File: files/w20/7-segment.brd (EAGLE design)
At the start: 37.5 x 64.8 mm, 18 parts

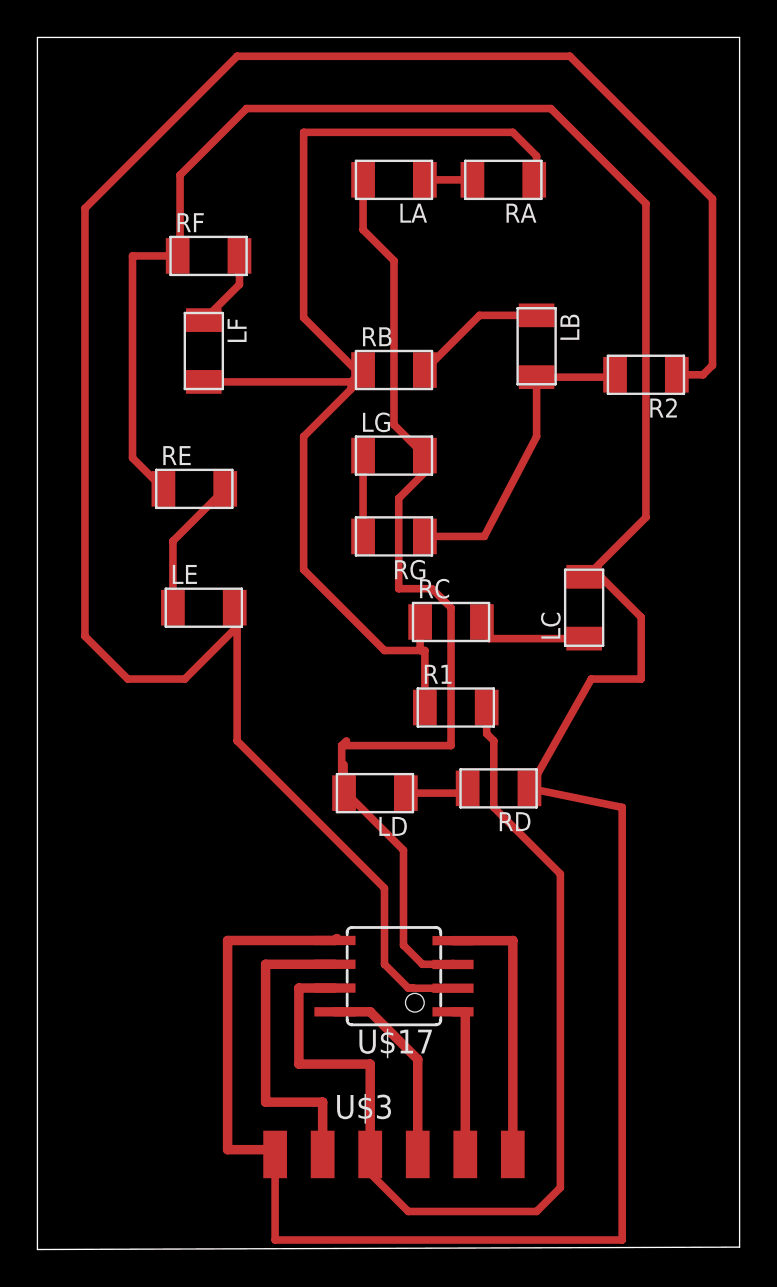
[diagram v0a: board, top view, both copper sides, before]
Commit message: board layout tweaks
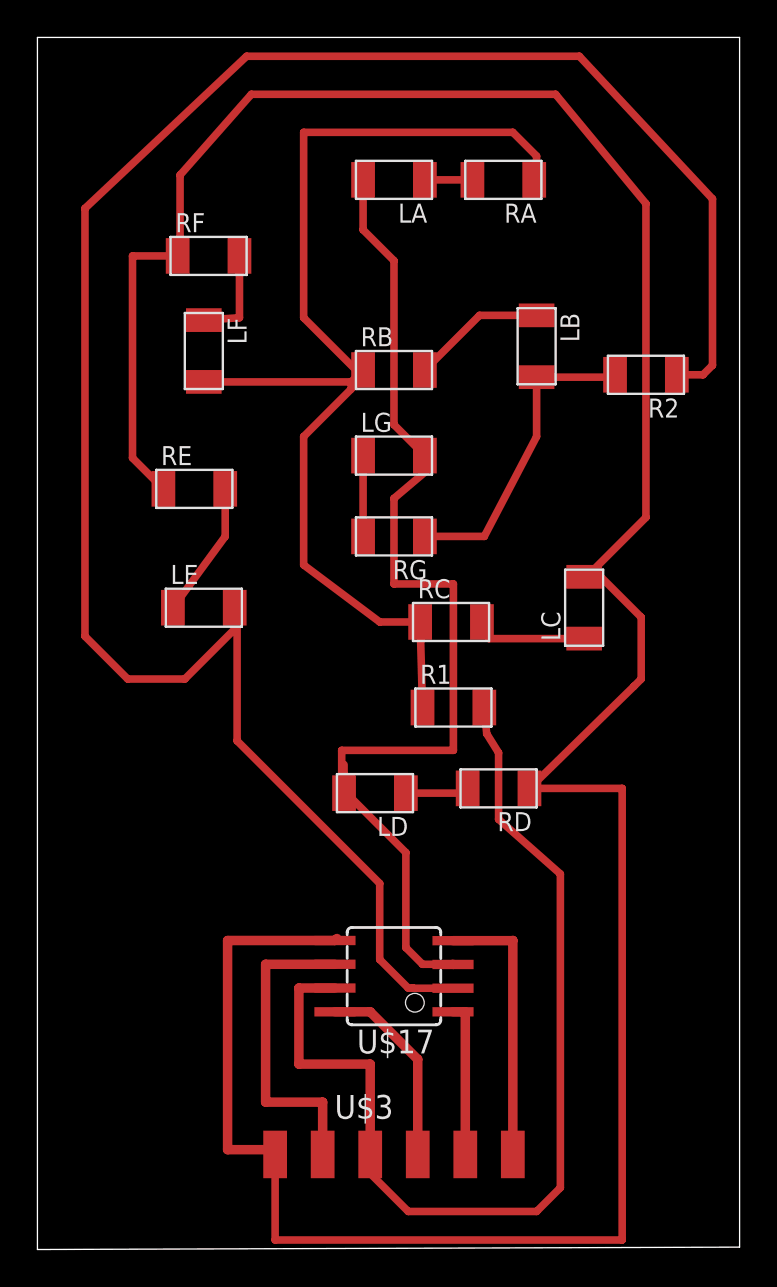
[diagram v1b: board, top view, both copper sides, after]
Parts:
- moved R1 0.13 mm to (20.4, 28.2)
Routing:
- net SCK: track 114.3 -> 113.1 mm
- net MOSI: track 157.4 -> 158.4 mm
- net N$6: track 4.22 -> 5.21 mm
- net PB4: track 56.3 -> 57.2 mm

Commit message: vias done
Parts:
- moved R2 10.8 mm to (27.6, 35.7)
- moved RE 9.11 mm to (7.10, 30.8)
- moved LE 8.94 mm to (11.1, 25.5), turned to 270 degrees
- moved LA 8.43 mm to (18.0, 48.0)
- moved RA 8.41 mm to (23.6, 48.0)
- moved LC 7.78 mm to (26.3, 25.8)
- moved LF 6.99 mm to (9.11, 40.5)
- moved LB 6.10 mm to (25.1, 41.4)
- moved RF 5.91 mm to (9.27, 46.7), turned to 270 degrees
- moved LG 5.05 mm to (18.0, 36.7)
- moved RG 4.75 mm to (18.0, 32.6)
- moved RC 4.44 mm to (18.0, 29.0)
- moved RD 4.20 mm to (23.1, 19.7)
- moved LD 4.00 mm to (16.3, 19.6)
- moved R1 4.00 mm to (18.0, 25.0)
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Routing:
- net MOSI: track 158.4 -> 147.1 mm
- net SCK: track 113.1 -> 102.1 mm
- net PB4: track 57.2 -> 48.7 mm
- net N$3: track 6.05 -> 9.23 mm
- net GND: track 14.6 -> 11.9 mm
- net RST: track 8.28 -> 5.58 mm
- net N$6: track 5.21 -> 3.06 mm
- net VCC: track 10.6 -> 8.70 mm
- net N$2: track 7.18 -> 5.47 mm
- net N$5: track 7.26 -> 5.91 mm
- net MISO: track 16.9 -> 15.8 mm
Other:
- board size 37.5 x 64.8 mm -> 28.5 x 55.8 mm

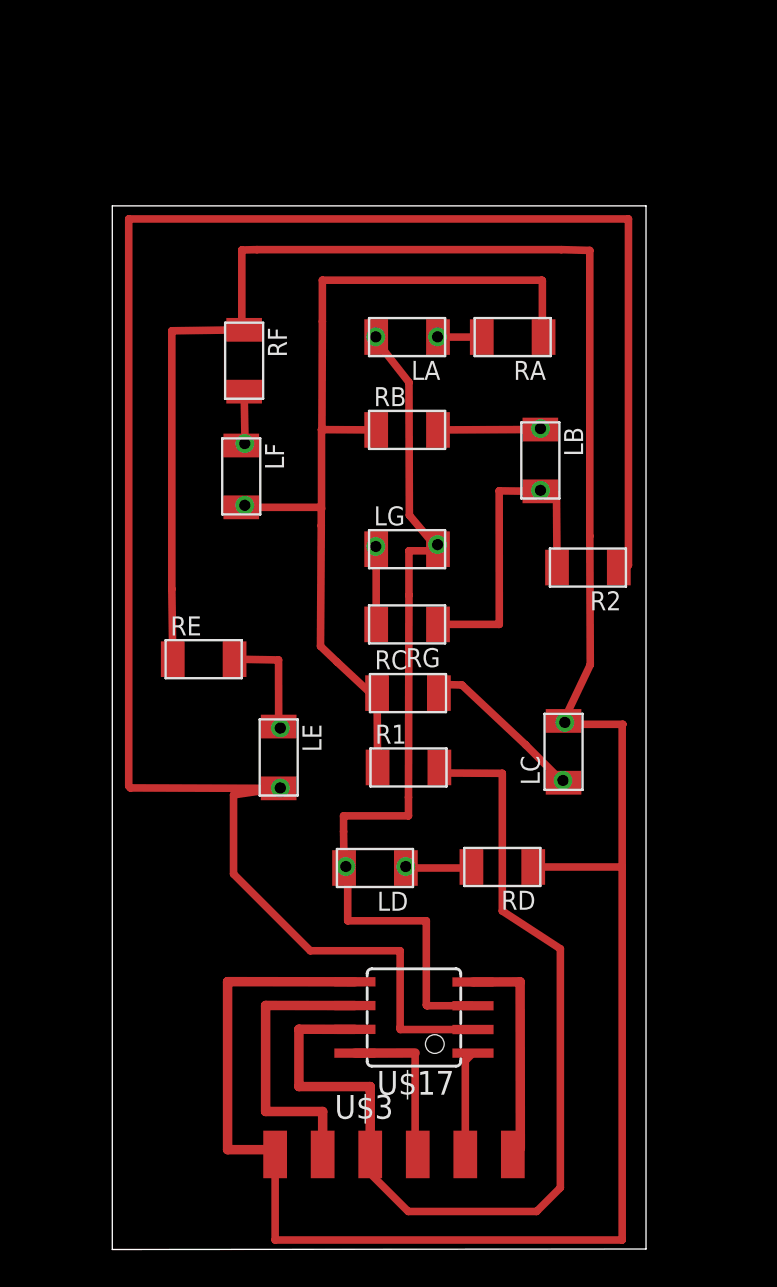
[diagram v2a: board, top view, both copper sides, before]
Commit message: 7segment board refactoring
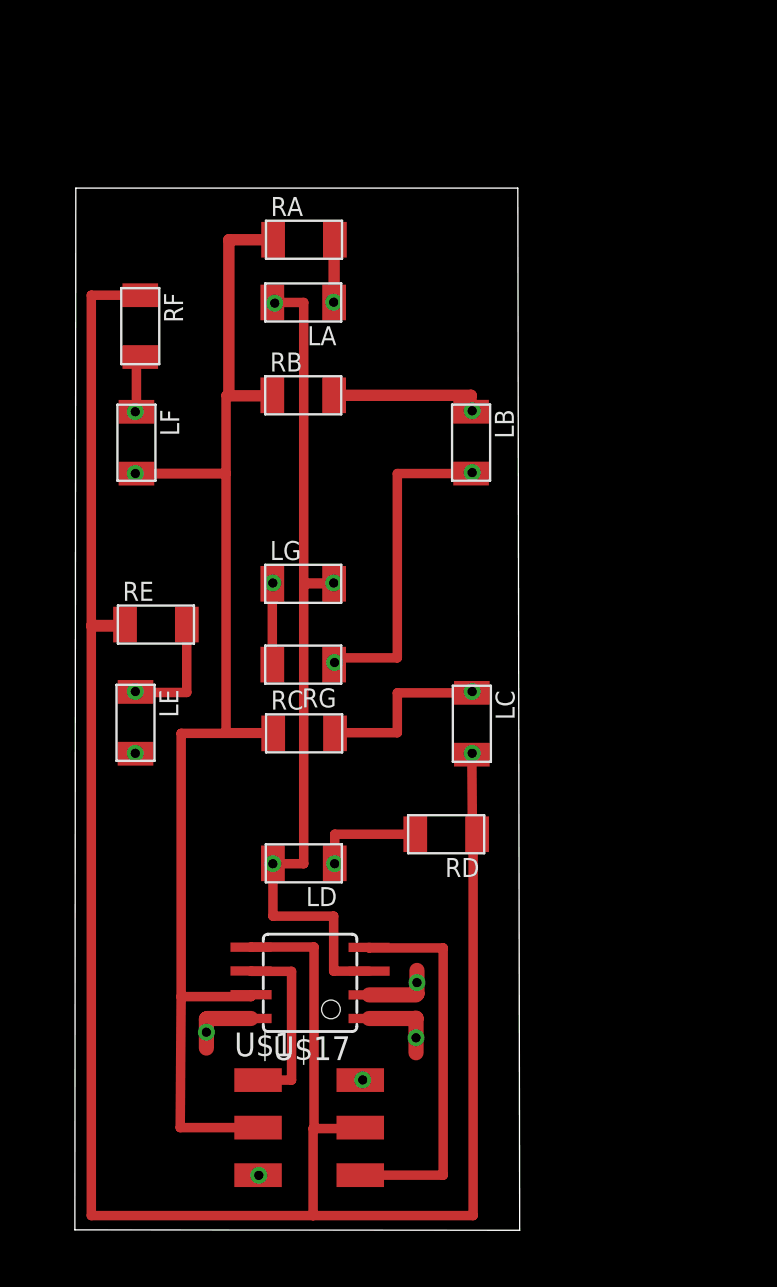
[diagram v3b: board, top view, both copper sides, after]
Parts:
- removed R1, R2: (no value), fab:R1206FAB
- removed U$3: FTDI-SMD-HEADER, fab:1X06SMD
- added U$1: AVRISPSMD, fab:2X03SMD
- moved RA 12.3 mm to (12.5, 53.2), turned to 0 degrees
- moved LE 7.87 mm to (3.46, 27.4)
- moved RG 5.95 mm to (12.4, 30.5)
- moved RC 5.95 mm to (12.5, 26.8)
- moved LF 5.88 mm to (3.51, 42.3)
- moved LA 5.85 mm to (12.4, 49.8)
- moved LG 5.85 mm to (12.4, 34.8)
- moved RB 5.85 mm to (12.4, 44.9)
- moved RF 5.85 mm to (3.72, 48.6)
- moved U$17 5.85 mm to (12.8, 13.5)
- moved LC 5.12 mm to (21.4, 27.3), turned to 270 degrees
- moved LB 3.82 mm to (21.4, 42.3)
- moved LD 3.81 mm to (12.5, 19.9)
- moved RD 3.47 mm to (20.1, 21.4)
- moved RE 3.15 mm to (4.55, 32.6)
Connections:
- net GND: now also U$1.6; no longer U$3.1
- net MISO: now also U$1.1; no longer U$3.5
- net MOSI: now also U$1.4; no longer U$3.6
- net PB3: no longer R2.1, R2.2
- net RST: now also U$1.5; no longer U$3.2
- net SCK: now also U$1.3; no longer R1.1, R1.2, U$3.4
- net VCC: now also U$1.2; no longer U$3.3
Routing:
- net PB3: track 126.8 -> 21.4 mm
- net MOSI: track 147.1 -> 121.5 mm
- net SCK: track 102.1 -> 79.7 mm
- net GND: track 11.9 -> 20.6 mm
- net MISO: track 15.8 -> 9.79 mm
- net VCC: track 8.70 -> 3.97 mm
- net N$2: track 5.47 -> 8.20 mm
- net N$4: track 3.63 -> 5.86 mm
- net RST: track 5.58 -> 4.38 mm
- net PB4: track 48.7 -> 47.5 mm, vias 0 -> 1
- net N$1: track 2.34 -> 3.39 mm
- net N$3: track 9.23 -> 9.99 mm
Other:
- board size 28.5 x 55.8 mm -> 23.8 x 55.7 mm
